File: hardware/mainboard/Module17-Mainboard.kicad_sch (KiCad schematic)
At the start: 7 parts

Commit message: Updated Mainboard PCB to revision 1.0
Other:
- company: M17Project -> M17 Project
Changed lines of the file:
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@@
 	(title_block
 		(title "Module17")
-		(date "2024-04-25")
-		(rev "Rev 0.99b")
-		(company "M17Project")
-		(comment 1 "Morgan ON4MOD")
+		(date "2024-06-19")
+		(rev "Rev 1.0")
+		(company "M17 Project")
+		(comment 1 "Morgan - ON4MOD")
 		(comment 2 "Mathis - DB9MAT")
 		(comment 3 "Wojciech - SP5WWP")

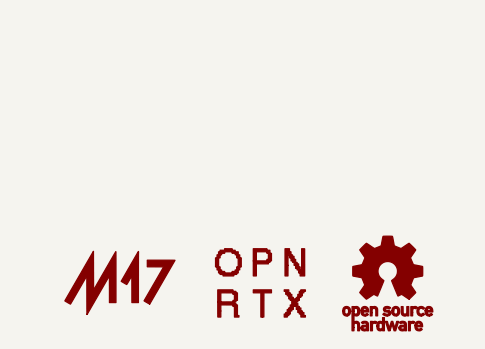
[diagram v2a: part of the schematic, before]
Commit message: Added OSHWA certification mark
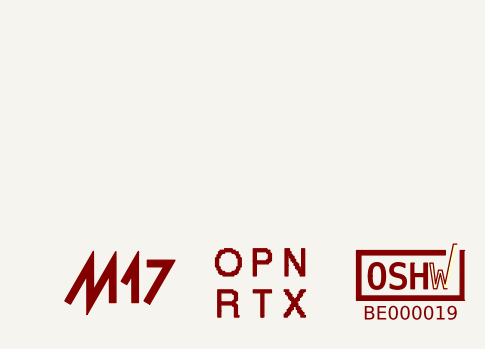
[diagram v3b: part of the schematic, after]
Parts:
- removed LOGO103: OSHW_logo, M17_logos:OSHW_logo_12.5x13mm, symbol M17_logos:OSHW_logo
- added LOGO104: ~, OSHW_Certification_Mark:OSHW-Certification-Mark-Stacked_12x10mm_SilkMask, symbol OSHW_Certification_Mark:OSHW_Certification_Mark_Stacked_Medium
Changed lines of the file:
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@@
 	)
 	(symbol
-		(lib_id "M17_logos:OSHW_logo")
-		(at 254.635 174.625 0)
+		(lib_id "OSHW_Certification_Mark:OSHW_Certification_Mark_Stacked_Medium")
+		(at 257.175 173.355 0)
 		(unit 1)
 		(exclude_from_sim no)
@@
 		(dnp no)
 		(fields_autoplaced yes)
-		(property "Reference" "LOGO103"
-			(at 254.635 170.0012 0)
+		(property "Reference" "LOGO104"
+			(at 257.175 173.355 0)
 			(effects
 				(font
@@
 			)
 		)
-		(property "Value" "OSHW_logo"
-			(at 254.635 179.2488 0)
+		(property "Value" "~"
+			(at 257.175 173.355 0)
 			(effects
 				(font
@@
 			)
 		)
-		(property "Footprint" "M17_logos:OSHW_logo_12.5x13mm"
-			(at 254.635 174.625 0)
+		(property "Footprint" "OSHW_Certification_Mark:OSHW-Certification-Mark-Stacked_12x10mm_SilkMask"
+			(at 257.175 173.355 0)
 			(effects
 				(font
@@
 		)
 		(property "Datasheet" ""
-			(at 254.635 174.625 0)
+			(at 257.175 173.355 0)
 			(effects
 				(font
@@
 			)
 		)
-		(property "Description" ""
-			(at 254.635 174.625 0)
+		(property "Description" "OSHW Certification Mark, Stacked"
+			(at 257.175 173.355 0)
 			(effects
 				(font
@@
 		)
 		(instances
-			(project "Module17-Mainboard"
+			(project ""
 				(path "/59592280-3207-432b-a891-cd517ec5cf12"
-					(reference "LOGO103")
+					(reference "LOGO104")
 					(unit 1)
 				)
